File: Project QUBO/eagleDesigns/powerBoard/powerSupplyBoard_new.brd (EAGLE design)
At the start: 152.4 x 101.6 mm, 137 parts

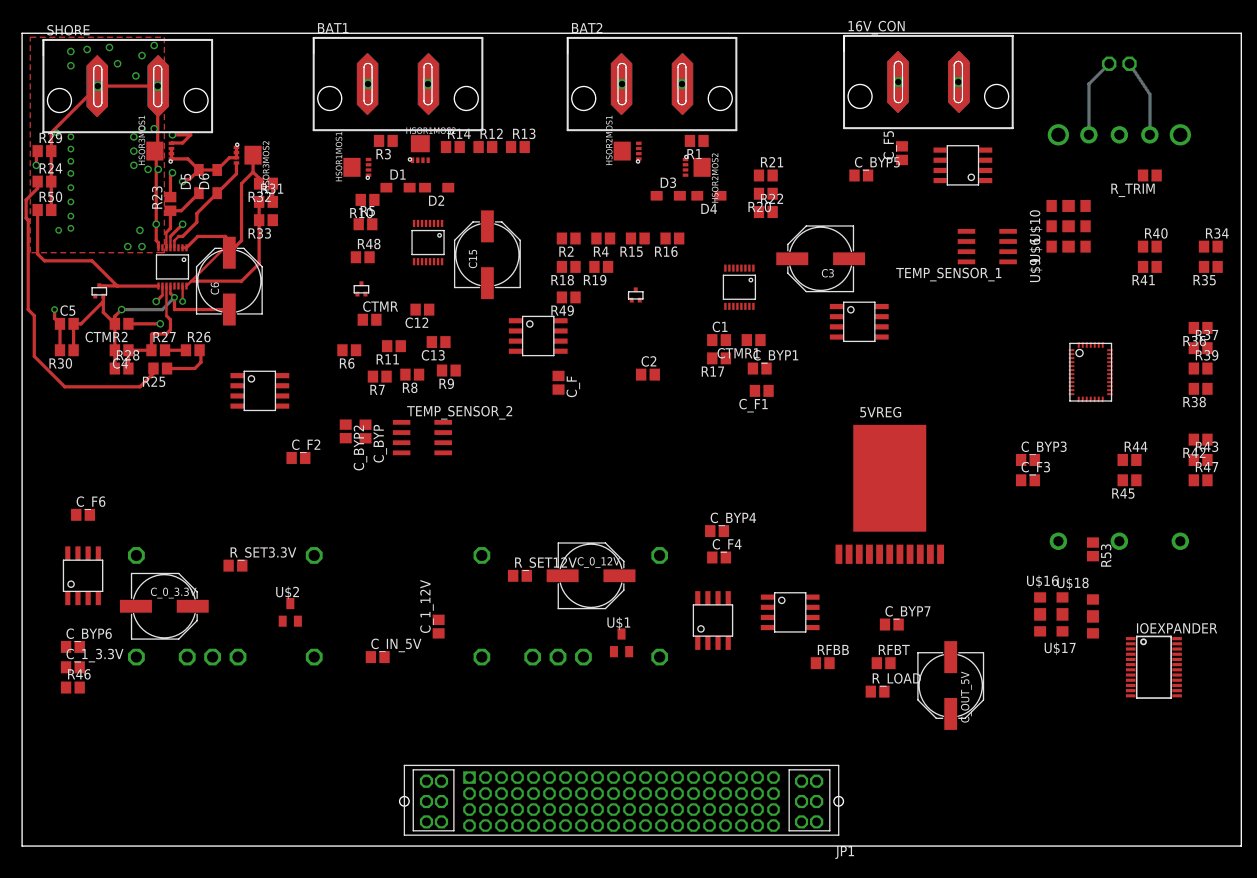
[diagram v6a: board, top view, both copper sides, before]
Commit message: 
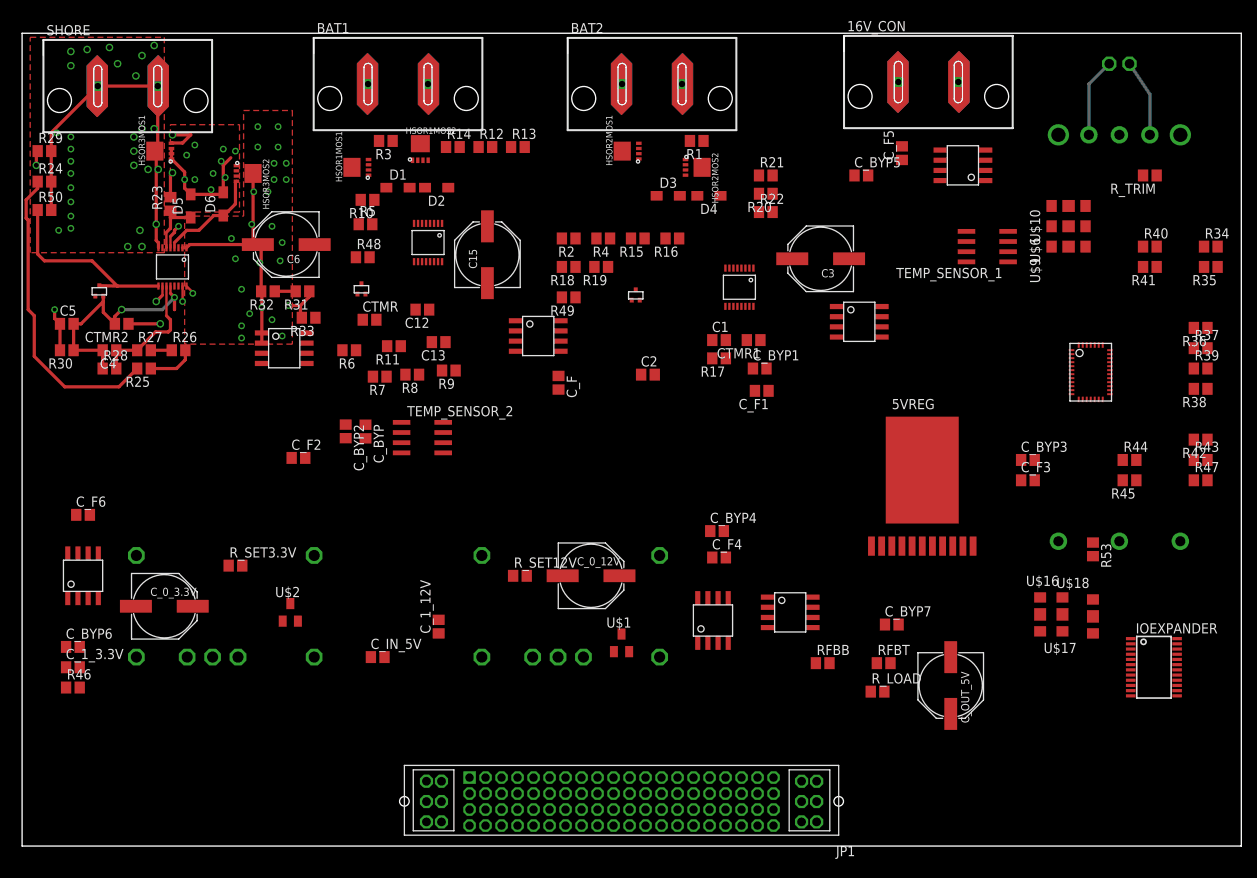
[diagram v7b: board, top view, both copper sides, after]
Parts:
- moved R32 13.5 mm to (30.7, 69.3)
- moved R33 13.3 mm to (35.8, 66.0)
- moved R31 12.1 mm to (35.1, 69.3), turned to 180 degrees
- moved C6 8.45 mm to (33.0, 75.2), turned to 180 degrees
- moved BAT3CS 6.14 mm to (32.8, 62.2)
- moved 5VREG 4.19 mm to (112.5, 47.0)
- moved D5 3.21 mm to (21.1, 80.0)
- moved D6 2.90 mm to (25.1, 80.3)
- moved HSOR3MOS2 2.29 mm to (28.2, 84.1)
- moved R25 2.03 mm to (15.2, 59.7)
- moved R27 1.78 mm to (15.2, 62.0)
- moved R26 1.78 mm to (19.6, 62.0)
- moved C4 1.52 mm to (10.9, 62.0)
- moved R28 1.52 mm to (10.9, 59.7)
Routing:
- net BAT3HSOROUT: track 22.9 -> 31.3 mm, vias 0 -> 23
- net AGND: track 37.2 -> 30.7 mm
- net N$40: track 25.3 -> 19.2 mm, vias 0 -> 2
- net N$33: track 40.6 -> 38.3 mm
- net N$11: track 23.5 -> 24.8 mm, vias 2 -> 11
- net N$30: track 9.31 -> 8.24 mm
- net N$31: track 14.1 -> 13.4 mm
- added copper zone on layer 1, net BAT3HSOROUT
- added copper zone on layer 15, net BAT3HSOROUT
- added copper zone on layer 2, net BAT3HSOROUT
- added copper zone on layer 1, net N$11
- added copper zone on layer 15, net N$11
- added copper zone on layer 2, net N$11

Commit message: 
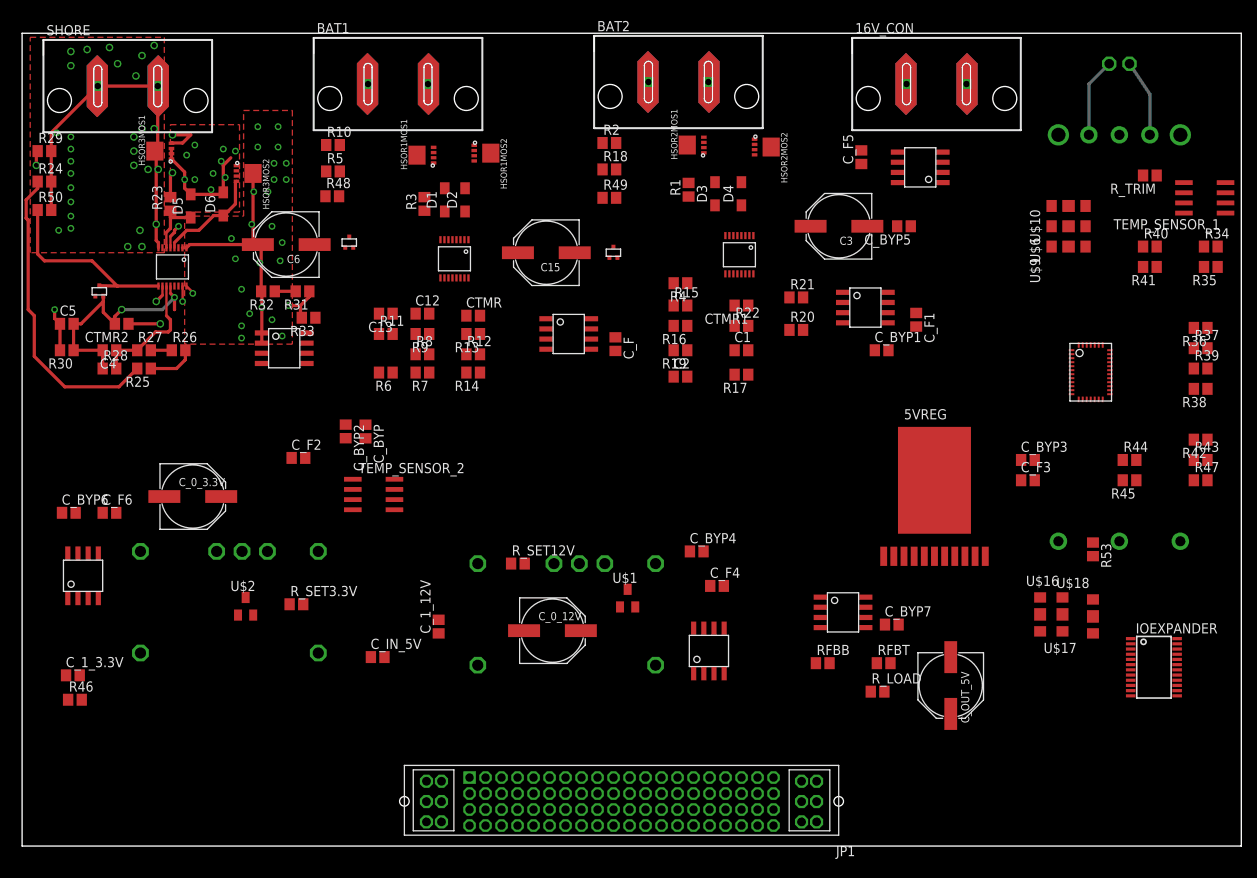
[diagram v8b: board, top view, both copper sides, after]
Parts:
- moved R14 28.3 mm to (56.4, 59.2), turned to 180 degrees
- moved TEMP_SENSOR_1 27.9 mm to (147.8, 81.0)
- moved R12 26.0 mm to (56.4, 61.5)
- moved R13 24.0 mm to (56.4, 64.0), turned to 180 degrees
- moved C_F1 21.3 mm to (111.8, 65.8), turned to 270 degrees
- moved R20 17.4 mm to (96.8, 64.5), turned to 0 degrees
- moved C_BYP6 16.8 mm to (5.84, 41.7)
- moved R21 15.7 mm to (96.8, 68.6)
- moved C_BYP1 15.4 mm to (107.4, 62.0)
- moved R22 14.5 mm to (89.9, 65.0)
- moved R19 14.4 mm to (82.3, 62.0)
- moved C_0_3.3V 14.2 mm to (21.3, 43.7)
- moved R49 13.4 mm to (73.4, 81.0), turned to 0 degrees
- moved R18 13.2 mm to (73.4, 84.6), turned to 0 degrees
- moved R2 13.0 mm to (73.4, 87.9), turned to 0 degrees
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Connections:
- new net N$1: JP1.P1,1, JP1.P1,2, JP1.P1,3, JP1.P1,4, JP1.P1,5, JP1.P1,6
- new net N$5: JP1.P2,1, JP1.P2,2, JP1.P2,3, JP1.P2,4, JP1.P2,5, JP1.P2,6
- net 16V: now also 16V_CON.P$1
- net AGND: no longer 16V_CON.P$1
